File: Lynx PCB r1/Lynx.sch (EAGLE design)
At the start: 108 parts, among them IC1 LM321MF, IC3 ICL7660, Q1 8MHz, X1 BU-SMA-V, X2 BU-SMA-V

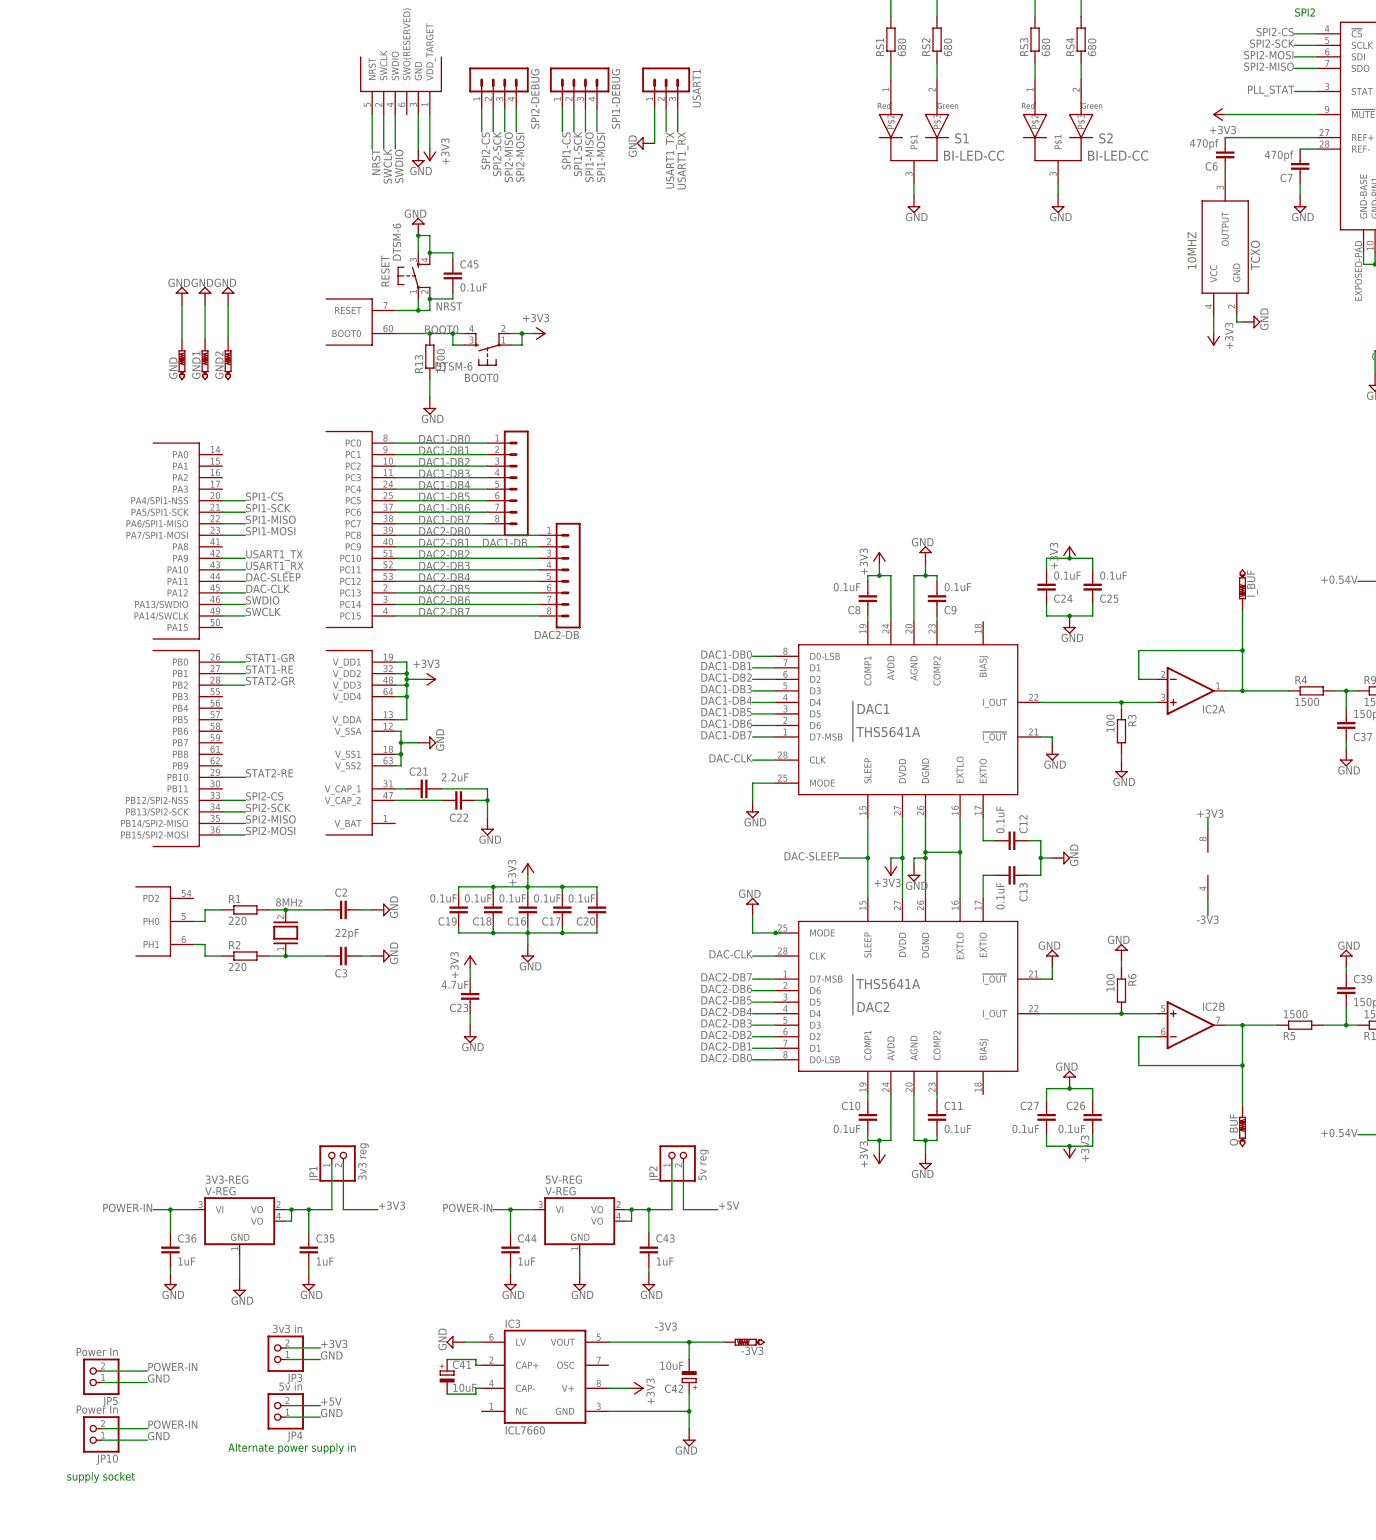
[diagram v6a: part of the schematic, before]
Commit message: Description text, pll-stat line
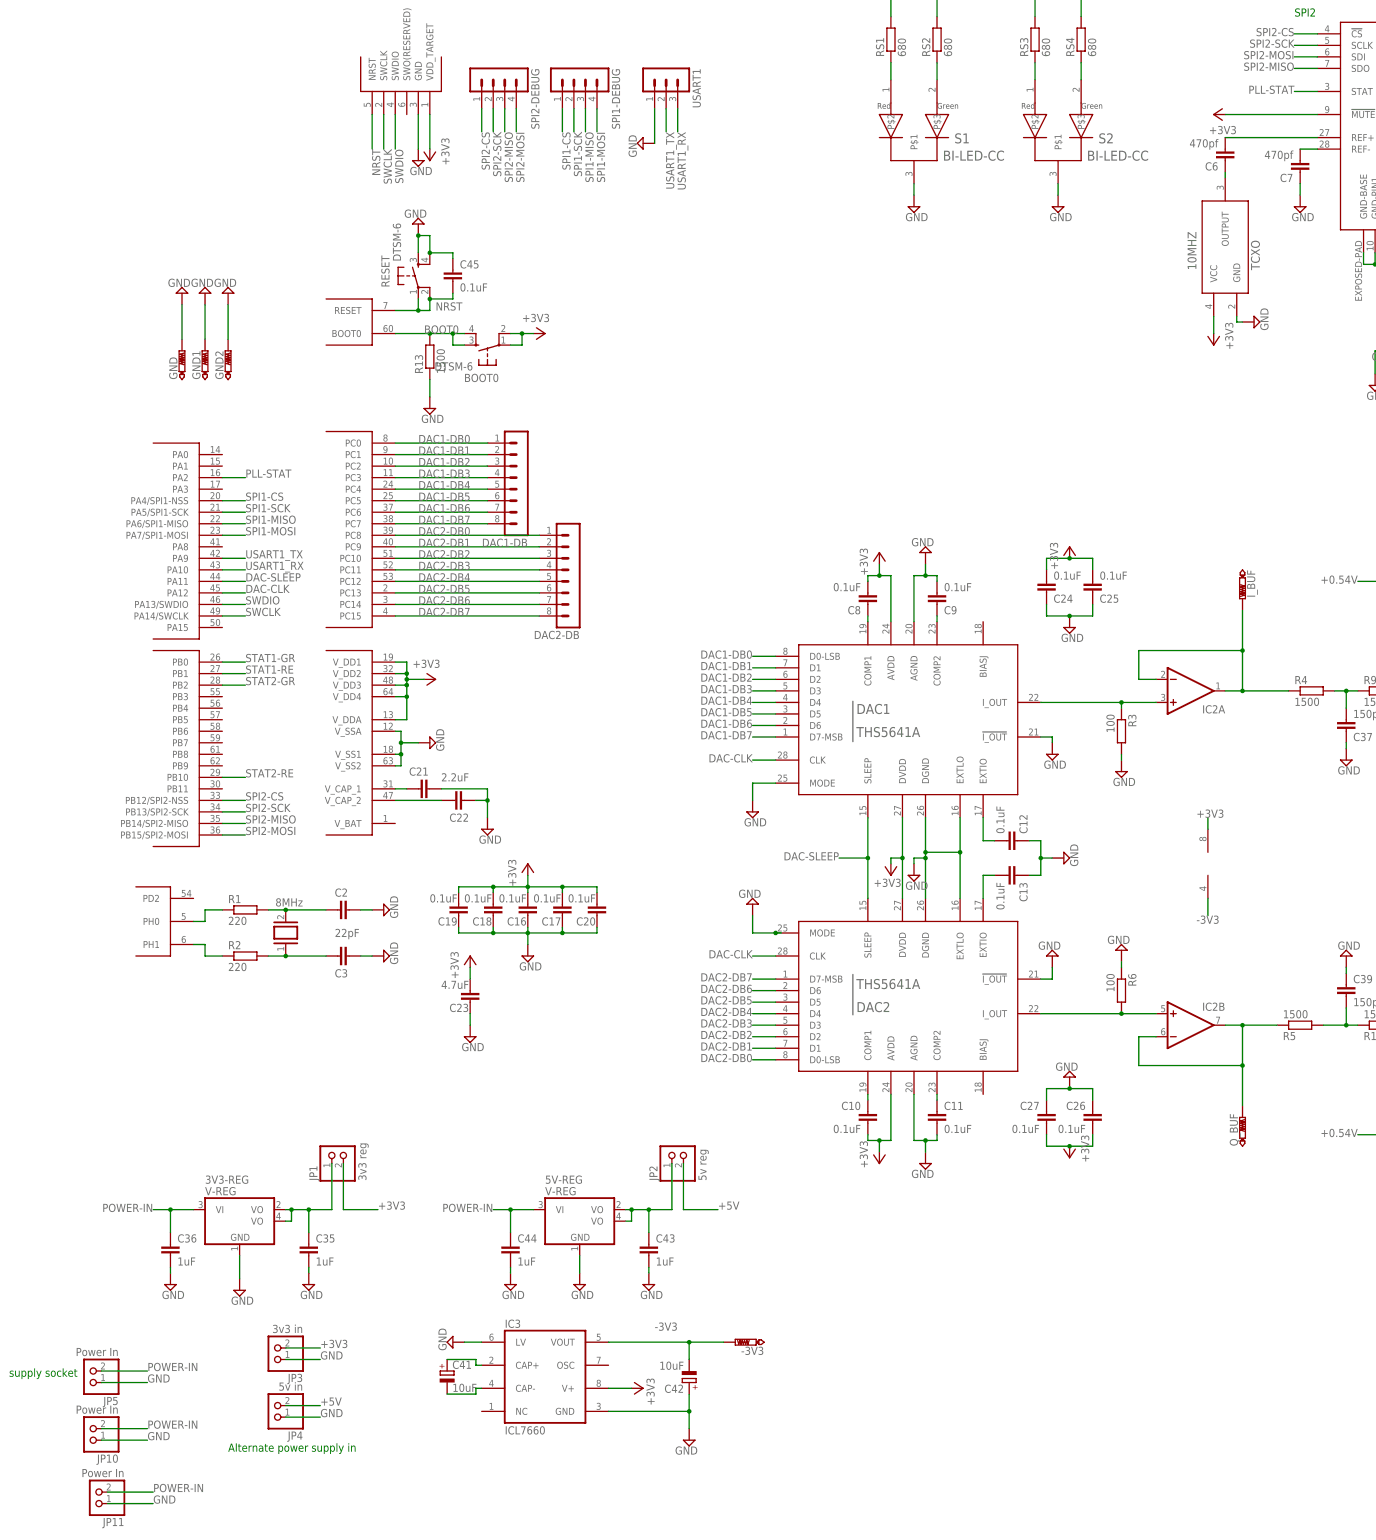
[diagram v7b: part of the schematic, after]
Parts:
- added JP11: Power In, pinhead:PINHD-1X2
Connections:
- removed net PLL_STAT: U$3.STAT
- new net PLL-STAT: U$1PORT_A.PA2, U$3.STAT
- net GND: now also JP11.1
- net POWER-IN: now also JP11.2
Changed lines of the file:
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@@
 <part name="SUPPLY58" library="supply2" deviceset="GND" device=""/>
 <part name="SUPPLY59" library="supply2" deviceset="GND" device=""/>
+<part name="JP11" library="pinhead" deviceset="PINHD-1X2" device="" value="Power In"/>
 </parts>
 <sheets>
@@
 <plain>
 <text x="-214.63" y="-160.02" size="1.778" layer="91">Alternate power supply in</text>
-<text x="-250.19" y="-166.37" size="1.778" layer="91">supply socket</text>
+<text x="-262.89" y="-143.51" size="1.778" layer="91">supply socket</text>
 <text x="20.32" y="156.21" size="1.778" layer="91">SPI2</text>
 </plain>
@@
 <instance part="SUPPLY58" gate="GND" x="63.5" y="-44.45" rot="MR0"/>
 <instance part="SUPPLY59" gate="GND" x="85.09" y="-44.45" rot="MR0"/>
+<instance part="JP11" gate="G$1" x="-243.84" y="-168.91" rot="R180"/>
 </instances>
 <busses>
@@
 <pinref part="SUPPLY59" gate="GND" pin="GND"/>
 <wire x1="85.09" y1="-41.91" x2="85.09" y2="-34.29" width="0.1524" layer="91"/>
+</segment>
+<segment>
+<pinref part="JP11" gate="G$1" pin="1"/>
+<wire x1="-241.3" y1="-171.45" x2="-231.14" y2="-171.45" width="0.1524" layer="91"/>
+<label x="-231.14" y="-171.45" size="1.778" layer="95"/>
 </segment>
 </net>
@@
 <label x="-232.41" y="-154.94" size="1.778" layer="95"/>
 </segment>
+<segment>
+<pinref part="JP11" gate="G$1" pin="2"/>
+<wire x1="-241.3" y1="-168.91" x2="-231.14" y2="-168.91" width="0.1524" layer="91"/>
+<label x="-231.14" y="-168.91" size="1.778" layer="95"/>
+</segment>
 </net>
 <net name="N$31" class="0">
@@
 </segment>
 </net>
-<net name="PLL_STAT" class="0">
-<segment>
-<pinref part="U$3" gate="G$1" pin="STAT"/>
-<wire x1="25.4" y1="139.7" x2="20.32" y2="139.7" width="0.1524" layer="91"/>
-<label x="20.32" y="140.97" size="1.778" layer="95" rot="R180"/>
-</segment>
-</net>
 <net name="N$3" class="0">
 <segment>
@@
 </segment>
 </net>
+<net name="PLL-STAT" class="0">
+<segment>
+<pinref part="U$1" gate="PORT_A" pin="PA2"/>
+<wire x1="-215.9" y1="54.61" x2="-210.82" y2="54.61" width="0.1524" layer="91"/>
+<label x="-210.82" y="54.61" size="1.778" layer="95"/>
+</segment>
+<segment>
+<pinref part="U$3" gate="G$1" pin="STAT"/>
+<wire x1="25.4" y1="139.7" x2="20.32" y2="139.7" width="0.1524" layer="91"/>
+<label x="20.32" y="140.97" size="1.778" layer="95" rot="R180"/>
+</segment>
+</net>

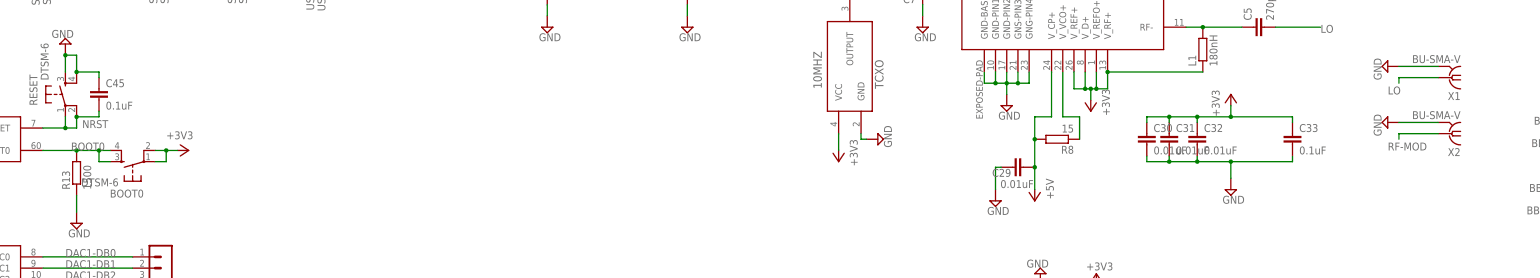
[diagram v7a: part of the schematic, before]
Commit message: started sorting out the silkscreen
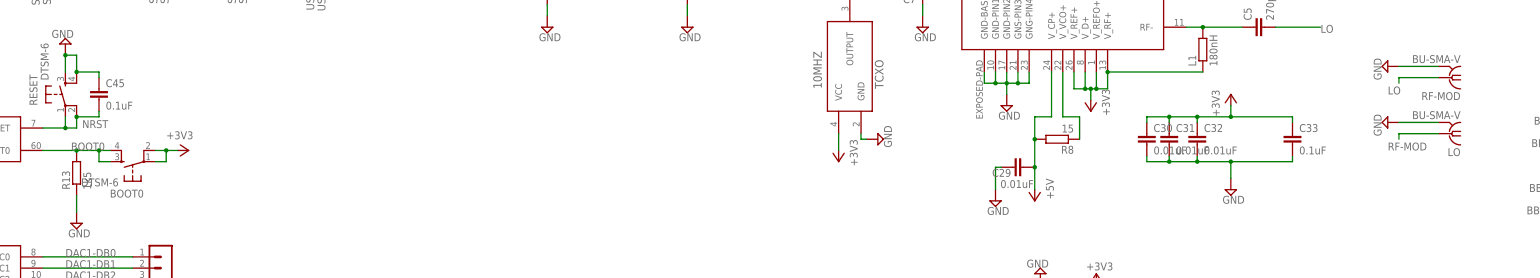
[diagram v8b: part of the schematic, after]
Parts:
- R13: value 1500 -> 1k5
- renumbered X1 to RF-MOD, X2 to LO
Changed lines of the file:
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@@
 <part name="SUPPLY34" library="supply2" deviceset="GND" device=""/>
 <part name="+3V12" library="supply1" deviceset="+3V3" device=""/>
-<part name="X1" library="con-coax" deviceset="BU-SMA-V" device=""/>
+<part name="RF-MOD" library="con-coax" deviceset="BU-SMA-V" device=""/>
 <part name="SUPPLY35" library="supply2" deviceset="GND" device=""/>
 <part name="R8" library="rcl" deviceset="R-EU_" device="R0603" value="15"/>
@@
 <part name="C45" library="rcl" deviceset="C-EU" device="C0603" value="0.1uF"/>
 <part name="+3V18" library="supply1" deviceset="+3V3" device=""/>
-<part name="R13" library="resistor" deviceset="R-EU_" device="R0603" value="1500"/>
+<part name="R13" library="resistor" deviceset="R-EU_" device="R0603" value="1k5"/>
 <part name="SUPPLY57" library="supply2" deviceset="GND" device=""/>
 <part name="BOOT0" library="switch-tact" deviceset="DTSM-6" device=""/>
-<part name="X2" library="con-coax" deviceset="BU-SMA-V" device=""/>
+<part name="LO" library="con-coax" deviceset="BU-SMA-V" device=""/>
 <part name="SUPPLY54" library="supply2" deviceset="GND" device=""/>
 <part name="+3V1" library="supply1" deviceset="+3V3" device=""/>
@@
 <instance part="SUPPLY34" gate="GND" x="-29.21" y="-77.47" rot="R180"/>
 <instance part="+3V12" gate="G$1" x="-29.21" y="-95.25" rot="R180"/>
-<instance part="X1" gate="G$1" x="140.97" y="102.87" rot="R180"/>
+<instance part="RF-MOD" gate="G$1" x="140.97" y="102.87" rot="R180"/>
 <instance part="SUPPLY35" gate="GND" x="127" y="105.41" rot="R270"/>
 <instance part="SUPPLY38" gate="GND" x="-212.09" y="-124.46"/>
@@
 <instance part="SUPPLY57" gate="GND" x="-170.18" y="69.85"/>
 <instance part="BOOT0" gate="G$1" x="-157.48" y="83.82" rot="R90"/>
-<instance part="X2" gate="G$1" x="140.97" y="90.17" rot="R180"/>
+<instance part="LO" gate="G$1" x="140.97" y="90.17" rot="R180"/>
 <instance part="SUPPLY54" gate="GND" x="127" y="92.71" rot="R270"/>
 <instance part="U$3" gate="G$1" x="63.5" y="142.24"/>
@@
 </segment>
 <segment>
-<pinref part="X1" gate="G$1" pin="2"/>
+<pinref part="RF-MOD" gate="G$1" pin="2"/>
 <wire x1="138.43" y1="105.41" x2="129.54" y2="105.41" width="0.1524" layer="91"/>
 <pinref part="SUPPLY35" gate="GND" pin="GND"/>
@@
 </segment>
 <segment>
-<pinref part="X2" gate="G$1" pin="2"/>
+<pinref part="LO" gate="G$1" pin="2"/>
 <wire x1="138.43" y1="92.71" x2="129.54" y2="92.71" width="0.1524" layer="91"/>
 <pinref part="SUPPLY54" gate="GND" pin="GND"/>
@@
 </segment>
 <segment>
-<pinref part="X1" gate="G$1" pin="1"/>
+<pinref part="RF-MOD" gate="G$1" pin="1"/>
 <wire x1="138.43" y1="102.87" x2="129.54" y2="102.87" width="0.1524" layer="91"/>
 <wire x1="129.54" y1="102.87" x2="129.54" y2="101.6" width="0.1524" layer="91"/>
@@
 </segment>
 <segment>
-<pinref part="X2" gate="G$1" pin="1"/>
+<pinref part="LO" gate="G$1" pin="1"/>
 <wire x1="138.43" y1="90.17" x2="129.54" y2="90.17" width="0.1524" layer="91"/>
 <wire x1="129.54" y1="90.17" x2="129.54" y2="88.9" width="0.1524" layer="91"/>
